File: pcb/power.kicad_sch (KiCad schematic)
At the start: 24 parts, among them J13 Power In, J2 USB_C_USB2.0_16P, U2 LM66200DRLR, U3 USBLC6-2P6, U6 LM66200DRLR, U7 AZ1084-3.3

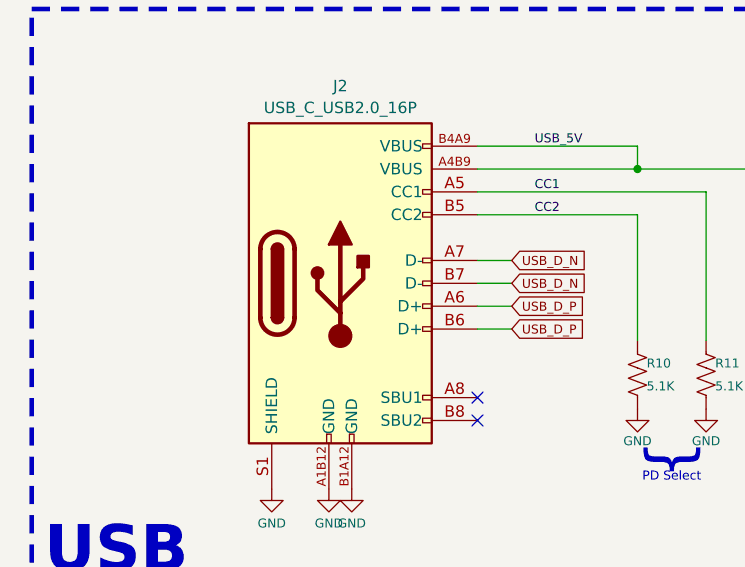
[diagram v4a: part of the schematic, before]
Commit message: Fixed MPN mismatches and other fields
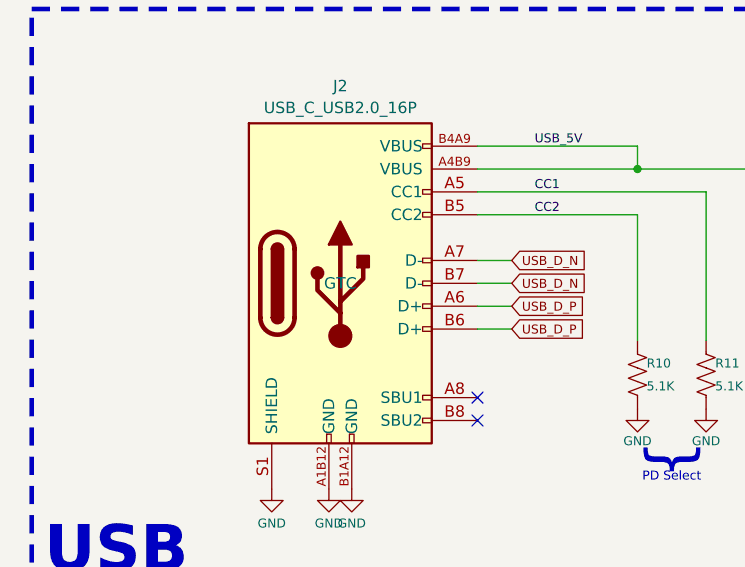
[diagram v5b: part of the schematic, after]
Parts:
- D20, D3: MF (none) -> Nexperia
- D23, D24: MF (none) -> XINGLIGHT
- D25: MF (none) -> FUXINSEMI; MN (none) -> FUXINSEMI
- J13: MF (none) -> JST
- J2: MF (none) -> GTC
- R15: MF (none) -> FOJAN
- R16: MF (none) -> Vishay
- U2, U6: MF (none) -> Texas Instruments
- U7: MF (none) -> Diodes Incorporated

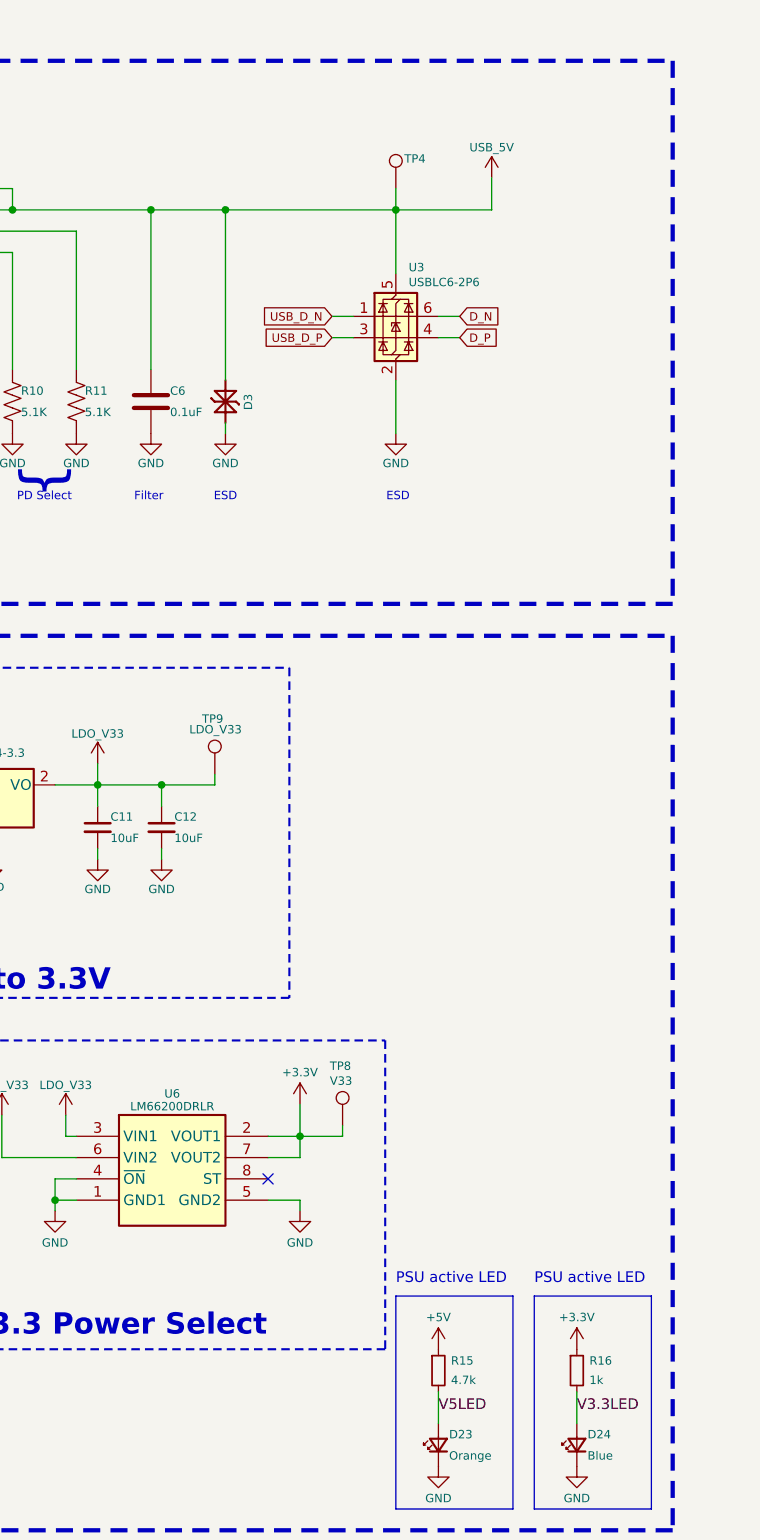
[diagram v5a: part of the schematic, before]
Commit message: Removed duplicative ESB on USB
Updated descriptions for consistency
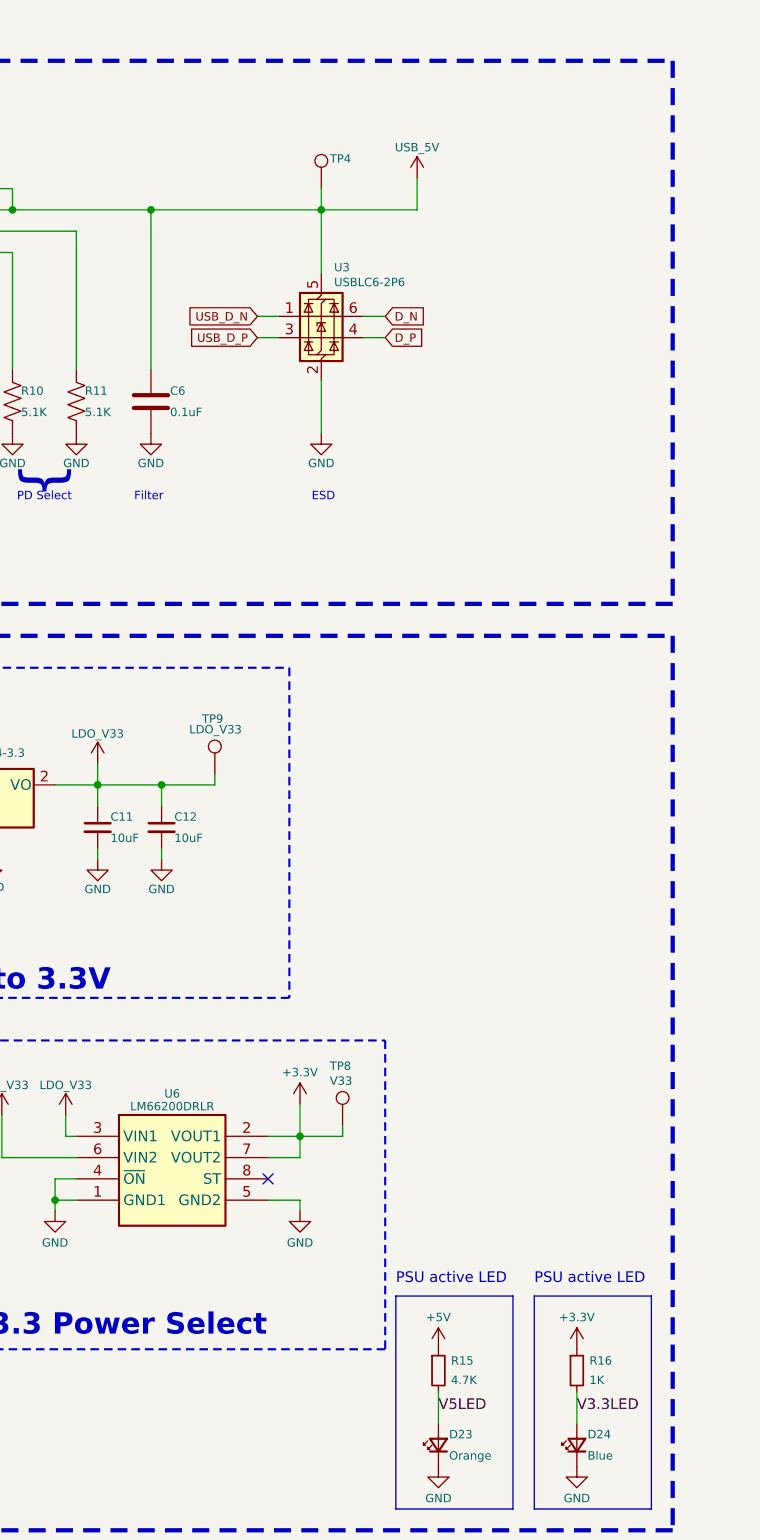
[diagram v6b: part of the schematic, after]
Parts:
- removed D3: PESD5V5C1BL, CRGM Passive:DFN1006-2, symbol CRGM Passive:PESD5V5C1BLYL
- R15: value 4.7k -> 4.7K
- R16: value 1k -> 1K
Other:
- moved on the sheet: TP4, U3

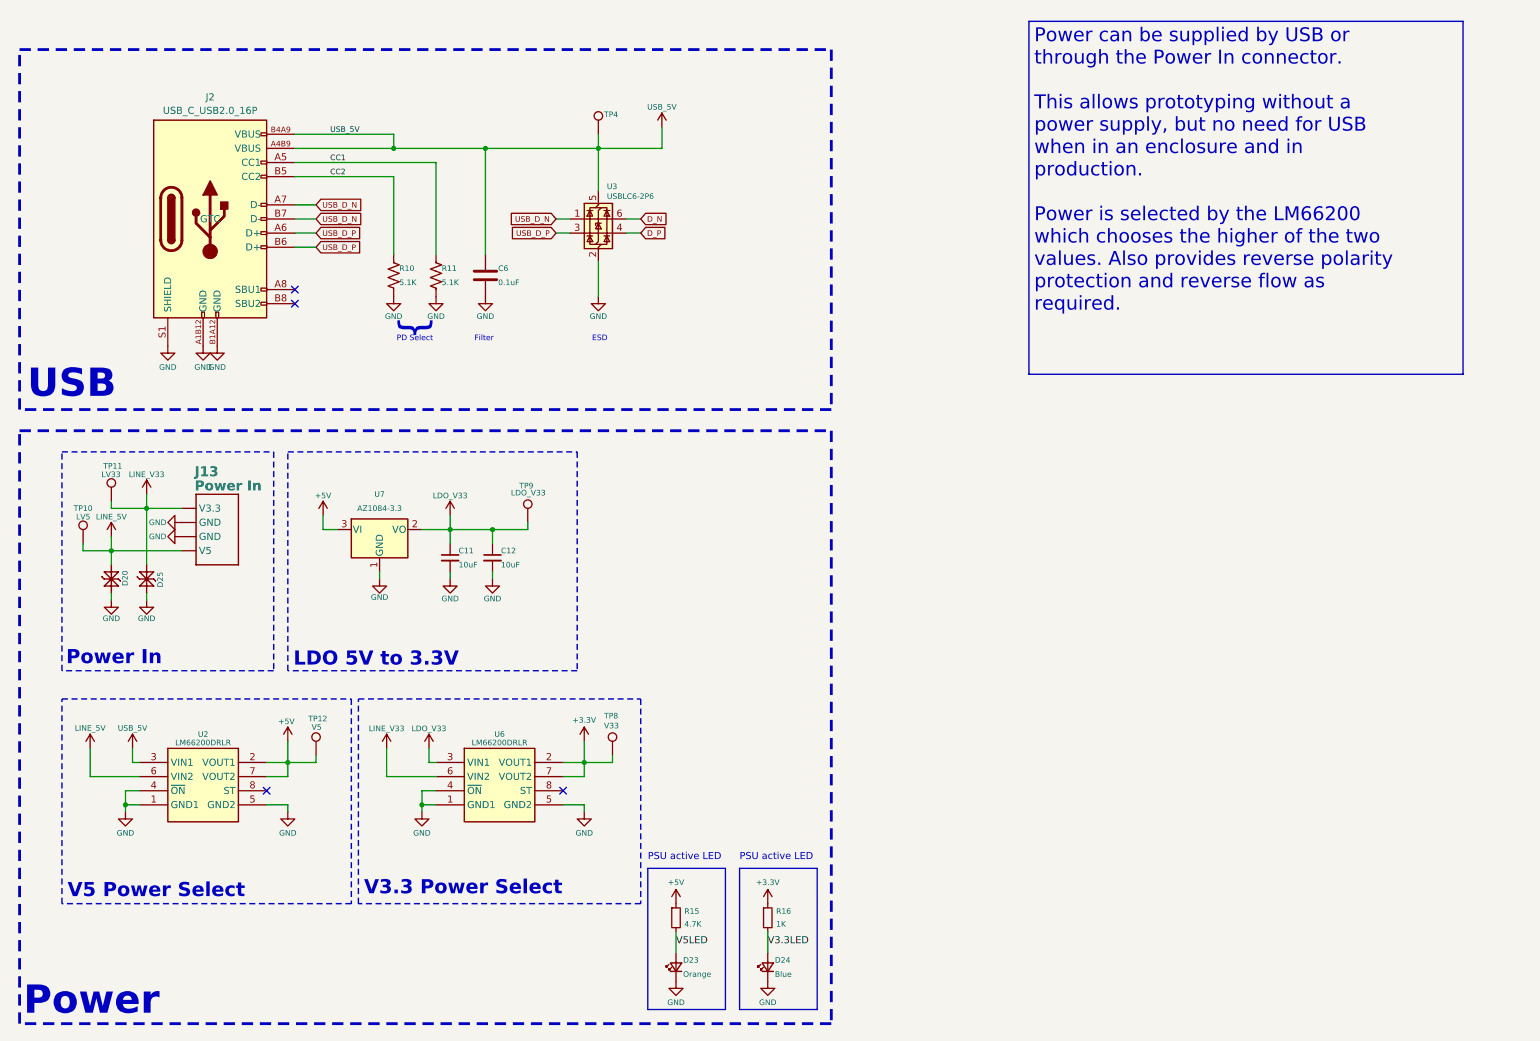
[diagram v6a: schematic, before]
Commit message: Fixed cap values on reset button
Fixed all part numbers and extended parameters.
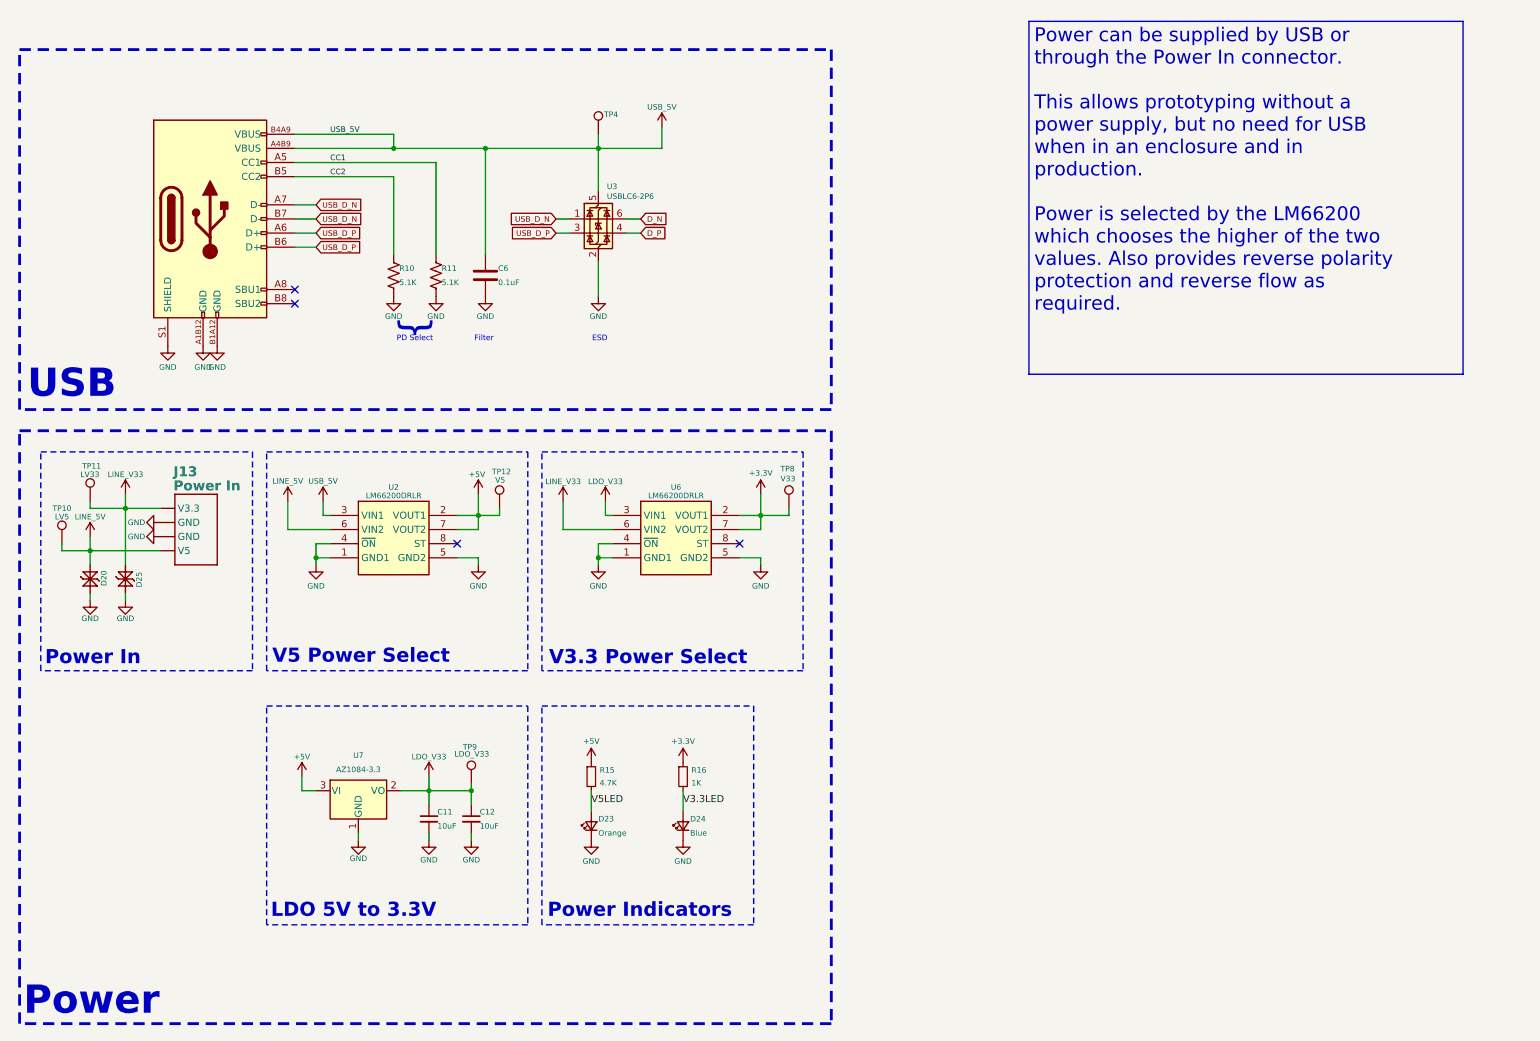
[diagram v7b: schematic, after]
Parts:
- C11, C12: MF Samsung -> (none)
- C6: Digikey (none) -> 1276-1005-2-ND; LCSC_PN C66501 -> (none); MF Samsung -> (none); Mouser (none) -> 187-CL10B104KO8NNNC
- D20: MF Nexperia -> (none)
- D23, D24: MF XINGLIGHT -> (none)
- D25: MF FUXINSEMI -> (none); MPN (none) -> LESD8D3.3CAT5G
- J13: MF JST -> (none)
- J2: MF GTC -> (none)
- R10, R11: Digikey (none) -> 118-CR0603-JW-512ELFTR-ND; LCSC_PN C2907114 -> (none); MF FOJAN -> (none); Mouser (none) -> 652-CR0603JW-512ELF
- R15: Digikey 541-3993-2-ND -> CR0603-JW-472ELFTR-ND; MF FOJAN -> (none); Mouser 71-CRCW06034K70JNEAC -> 652-CR0603-JW-472ELF
- R16: Digikey 541-1.00KHTR-ND -> CR0603-JW-102ELFTR-ND; MF Vishay -> (none); MN Vishay -> FOJAN; MPN CRCW06031K00FKEA -> FRC0603J102 TS; Mouser 71-CRCW0603-1.0K-E3 -> 652-CR0603-JW-102ELF
- U2, U6: LCSC_PN C3235556 -> (none); MF Texas Instruments -> (none)
- U3: Digikey (none) -> 497-5026-2-ND; LCSC_PN C2827693 -> (none); MF TECH PUBLIC -> (none); Mouser (none) -> 511-USBLC6-2P6
- U7: MF Diodes Incorporated -> (none)
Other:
- note added: "Power Indicators"
- note removed: "PSU active LED"
- moved on the sheet: C11, C12, D20, D23, D24, D25, J13, R15, R16, TP10, TP11, TP12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

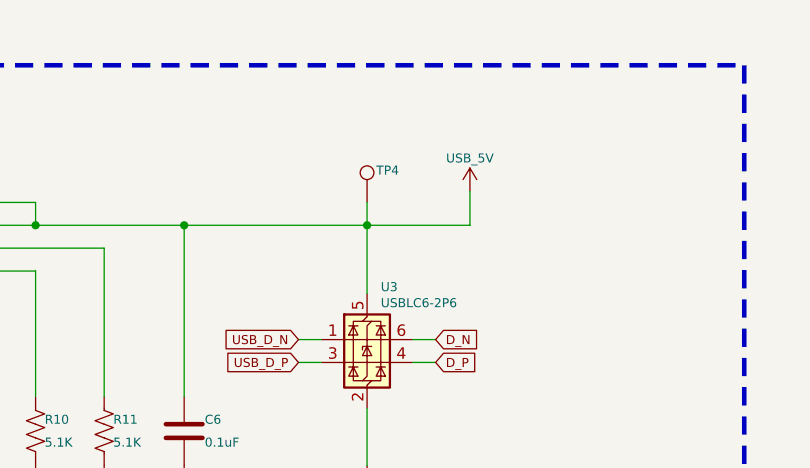
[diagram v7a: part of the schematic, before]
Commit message: Rationalized attributes; excluded some footprints from BOM
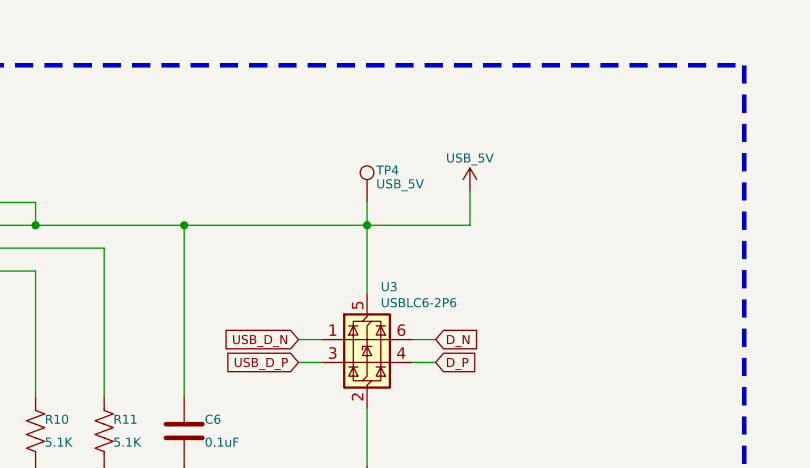
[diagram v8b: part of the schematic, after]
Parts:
- TP10, TP11, TP4: now left out of the parts list
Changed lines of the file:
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@@
 		(unit 1)
 		(exclude_from_sim no)
-		(in_bom yes)
+		(in_bom no)
 		(on_board yes)
 		(dnp no)
@@
 		(unit 1)
 		(exclude_from_sim no)
-		(in_bom yes)
+		(in_bom no)
 		(on_board yes)
 		(dnp no)
@@
 		(unit 1)
 		(exclude_from_sim no)
-		(in_bom yes)
+		(in_bom no)
 		(on_board yes)
 		(dnp no)
@@
 				)
 				(justify left)
-				(hide yes)
 			)
 		)
@@
 			(at 128.27 35.56 0)
 			(effects
+				(font
+					(size 1.27 1.27)
+				)
+				(hide yes)
+			)
+		)
+		(property "LCSC" ""
+			(at 128.27 35.56 0)
+			(effects
+				(font
+					(size 1.27 1.27)
+				)
+				(hide yes)
+			)
+		)
+		(property "Digikey" ""
+			(at 128.27 35.56 0)
+			(effects
+				(font
+					(size 1.27 1.27)
+				)
+				(hide yes)
+			)
+		)
+		(property "Mouser" ""
+			(at 128.27 35.56 0)
+			(effects
